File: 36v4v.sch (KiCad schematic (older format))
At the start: 47 parts, among them J1 Conn_01x03, J2 Conn_01x02, J3 Conn_01x02, J4 Conn_01x02, J5 Conn_01x02, J6 Conn_01x02, J7 Conn_01x02, U1 InnoSwitch3-CE, INN3162C, inS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

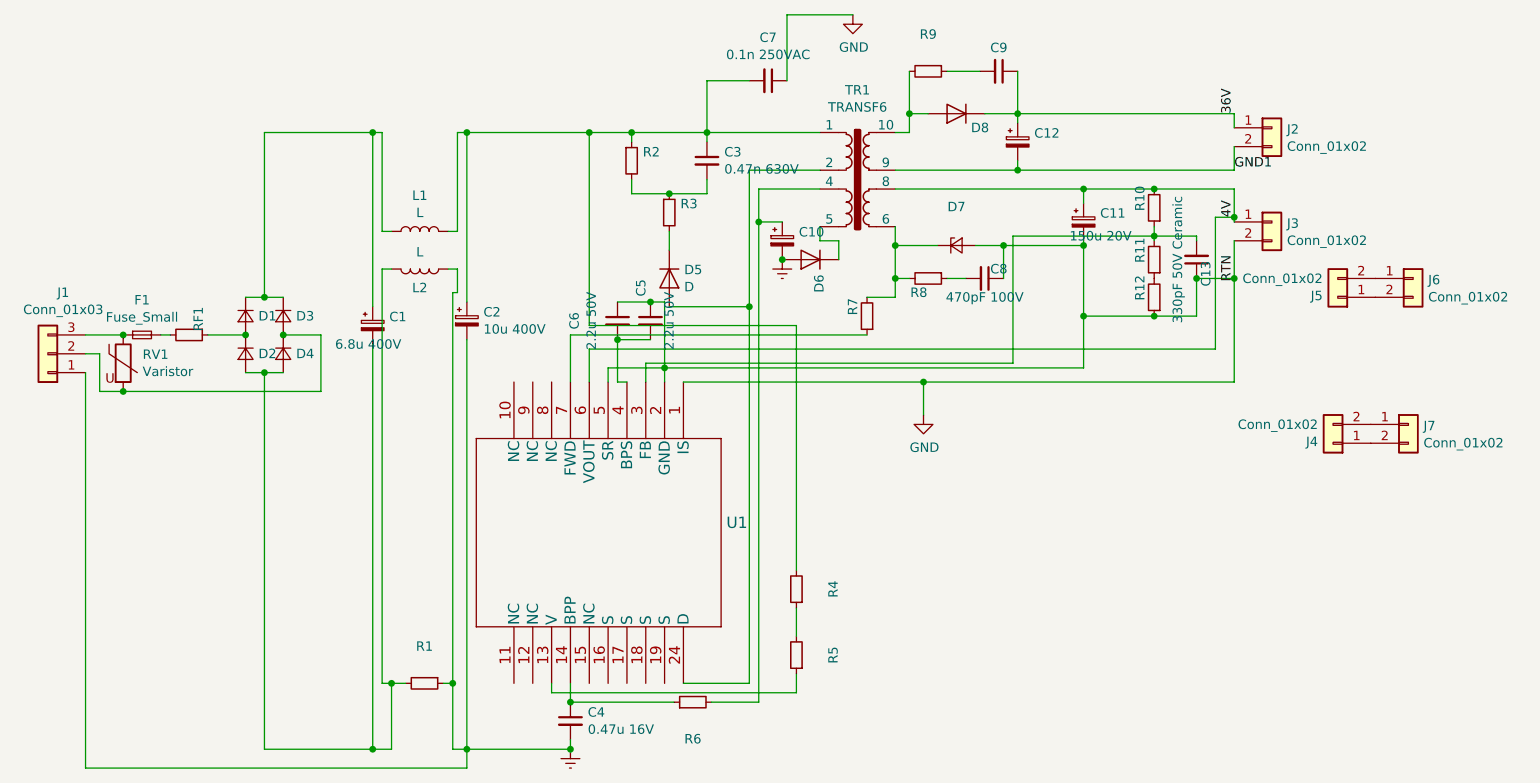
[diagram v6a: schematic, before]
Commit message: Rotated U1 in schematic to make primary/secondary clearer
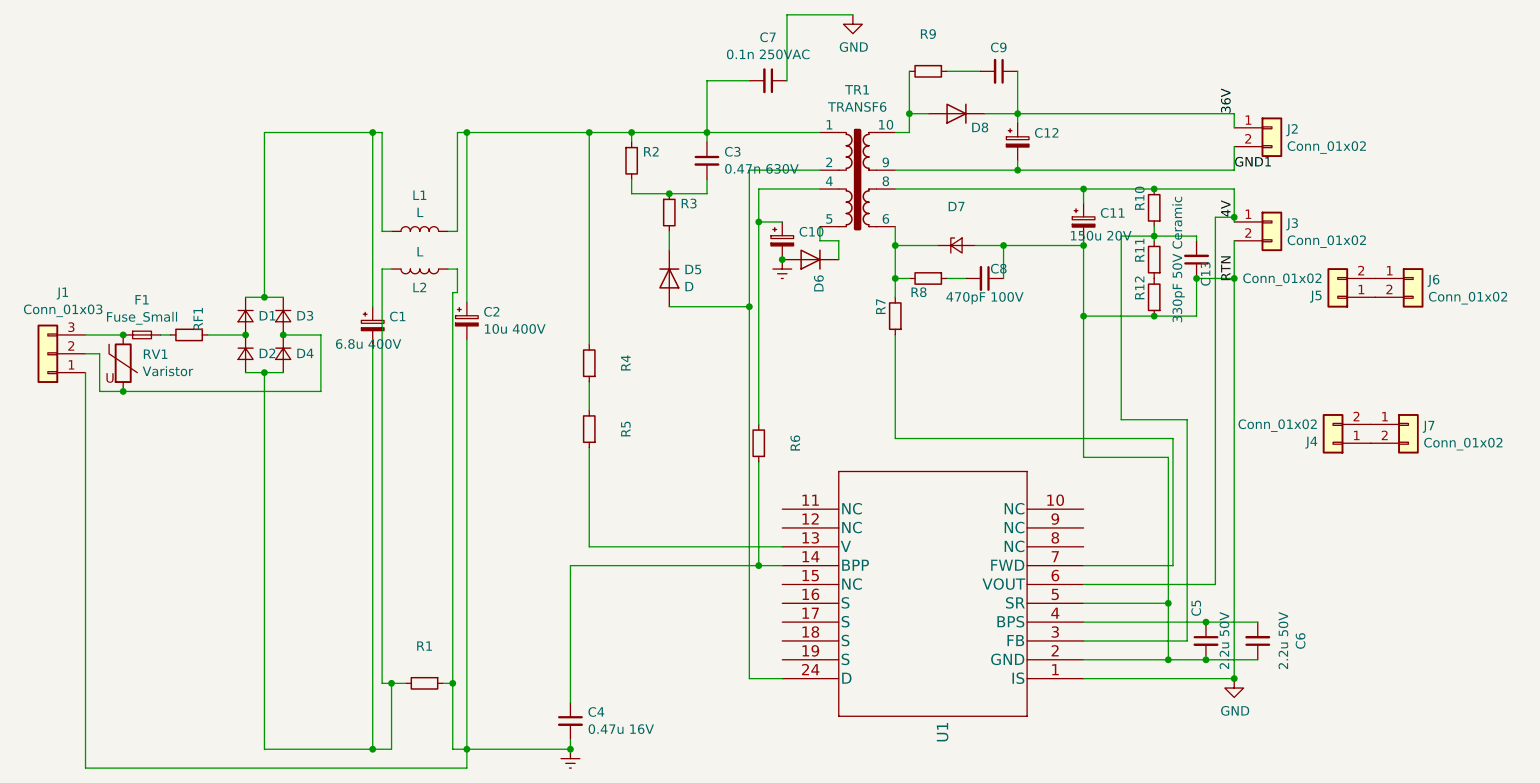
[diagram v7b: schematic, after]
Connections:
- net GND: now also C5.2; no longer C5.1
- net at C6.2, U1.4 (BPS): now also C5.1; no longer C5.2
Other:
- moved on the sheet: C5, C6, R4, R5, R6, R7
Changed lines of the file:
@@
 L Device:R_Small R7
 U 1 1 5E4F71AC
-P 6025 2425
-F 0 "R7" V 6100 2375 50  0000 C CNN
-F 1 "47 Ω, 5 %, 0.125 W, Carbon Film" V 5920 2425 50  0001 C CNN
-F 2 "Resistor_SMD:R_0603_1608Metric_Pad1.05x0.95mm_HandSolder" H 6025 2425 50  0001 C CNN
-F 3 "~" H 6025 2425 50  0001 C CNN
-	1    6025 2425
+P 6175 2425
+F 0 "R7" V 6250 2375 50  0000 C CNN
+F 1 "47 Ω, 5 %, 0.125 W, Carbon Film" V 6070 2425 50  0001 C CNN
+F 2 "Resistor_SMD:R_0603_1608Metric_Pad1.05x0.95mm_HandSolder" H 6175 2425 50  0001 C CNN
+F 3 "~" H 6175 2425 50  0001 C CNN
+	1    6175 2425
 	-1   0    0    1
 $EndComp
@@
 Text Label 7975 2100 3    50   ~ 0
 RTN
-$Comp
-L 2020-03-04_17-44-24:INN3162C-H1XX U1
-U 1 1 5E60AC5A
-P 5050 2775
-F 0 "U1" V 5797 3003 60  0000 L CNN
-F 1 "InnoSwitch3-CE, INN3162C, inSOP-24D" V 5903 3003 60  0001 L CNN
-F 2 "footprints:INN3162C-H1XX" H 5850 3015 60  0001 C CNN
-F 3 "" H 5050 2775 60  0000 C CNN
-F 4 "Power Integrations" H 5050 2775 50  0001 C CNN "MFG Name"
-F 5 "INN3162C-H101" H 5050 2775 50  0001 C CNN "MFG Part Num"
-	1    5050 2775
-	0    1    1    0
-$EndComp
 Wire Wire Line
 	3900 4725 4450 4725
@@
 Connection ~ 3900 4725
 Wire Wire Line
-	4450 4475 4450 4375
-Wire Wire Line
 	3900 2550 3900 4725
 Wire Wire Line
 	3400 2575 3400 4725
-Wire Wire Line
-	5050 4375 5400 4375
-Wire Wire Line
-	5400 4375 5400 2375
 $Comp
 L Device:R_Small R5
 U 1 1 5E66D184
-P 5650 4225
-F 0 "R5" V 5454 4225 50  0000 C CNN
-F 1 "1.78 MΩ, 1 %, 0.25 W, Metal Film" V 5545 4225 50  0001 C CNN
-F 2 "Resistor_SMD:R_0805_2012Metric_Pad1.15x1.40mm_HandSolder" H 5650 4225 50  0001 C CNN
-F 3 "~" H 5650 4225 50  0001 C CNN
-	1    5650 4225
+P 4550 3025
+F 0 "R5" V 4354 3025 50  0000 C CNN
+F 1 "1.78 MΩ, 1 %, 0.25 W, Metal Film" V 4445 3025 50  0001 C CNN
+F 2 "Resistor_SMD:R_0805_2012Metric_Pad1.15x1.40mm_HandSolder" H 4550 3025 50  0001 C CNN
+F 3 "~" H 4550 3025 50  0001 C CNN
+	1    4550 3025
 	-1   0    0    1
 $EndComp
@@
 L Device:R_Small R4
 U 1 1 5E66D7F4
-P 5650 3875
-F 0 "R4" V 5454 3875 50  0000 C CNN
-F 1 "1.78 MΩ, 1 %, 0.25 W, Metal Film" V 5545 3875 50  0001 C CNN
-F 2 "Resistor_SMD:R_0805_2012Metric_Pad1.15x1.40mm_HandSolder" H 5650 3875 50  0001 C CNN
-F 3 "~" H 5650 3875 50  0001 C CNN
-	1    5650 3875
-	-1   0    0    1
-$EndComp
-Wire Wire Line
-	5650 4125 5650 3975
-Wire Wire Line
-	5650 3775 5650 2475
-Wire Wire Line
-	5650 2475 4550 2475
-Wire Wire Line
-	4550 2475 4550 1450
+P 4550 2675
+F 0 "R4" V 4354 2675 50  0000 C CNN
+F 1 "1.78 MΩ, 1 %, 0.25 W, Metal Film" V 4445 2675 50  0001 C CNN
+F 2 "Resistor_SMD:R_0805_2012Metric_Pad1.15x1.40mm_HandSolder" H 4550 2675 50  0001 C CNN
+F 3 "~" H 4550 2675 50  0001 C CNN
+	1    4550 2675
+	-1   0    0    1
+$EndComp
+Wire Wire Line
+	4550 2925 4550 2775
 Connection ~ 4550 1450
 Wire Wire Line
 	4550 1450 4775 1450
-Wire Wire Line
-	4350 4375 4350 4425
-Wire Wire Line
-	4350 4425 5650 4425
-Wire Wire Line
-	5650 4425 5650 4325
 $Comp
 L Device:R_Small R6
 U 1 1 5E68331A
-P 5100 4475
-F 0 "R6" V 4904 4475 50  0000 C CNN
-F 1 "14 kΩ, 1 %, 0.125 W, Metal Film" V 4995 4475 50  0001 C CNN
-F 2 "Resistor_SMD:R_0805_2012Metric_Pad1.15x1.40mm_HandSolder" H 5100 4475 50  0001 C CNN
-F 3 "~" H 5100 4475 50  0001 C CNN
-	1    5100 4475
-	0    -1   -1   0
-$EndComp
-Wire Wire Line
-	4450 4475 5000 4475
-Connection ~ 4450 4475
-Wire Wire Line
-	5200 4475 5450 4475
-Wire Wire Line
-	5450 4475 5450 1925
+P 5450 3100
+F 0 "R6" V 5254 3100 50  0000 C CNN
+F 1 "14 kΩ, 1 %, 0.125 W, Metal Film" V 5345 3100 50  0001 C CNN
+F 2 "Resistor_SMD:R_0805_2012Metric_Pad1.15x1.40mm_HandSolder" H 5450 3100 50  0001 C CNN
+F 3 "~" H 5450 3100 50  0001 C CNN
+	1    5450 3100
+	-1   0    0    1
+$EndComp
+Wire Wire Line
+	5450 3750 5450 3200
 $Comp
 L Device:CP_Small C10
@@
 	6825 1350 7975 1350
 Wire Wire Line
-	4550 2775 4550 2600
-Wire Wire Line
-	4550 2600 7875 2600
-Wire Wire Line
-	7875 2600 7875 1900
-Wire Wire Line
 	7875 1900 7975 1900
 Wire Wire Line
@@
 	6600 2050 6750 2050
 Wire Wire Line
-	4450 2775 4450 2525
-Wire Wire Line
-	4450 2525 6025 2525
-Wire Wire Line
-	6025 2325 6175 2325
-Wire Wire Line
 	6175 2325 6175 2225
 Connection ~ 6175 2225
@@
 Connection ~ 6750 2050
 Connection ~ 7175 2050
-Wire Wire Line
-	4950 2700 7175 2700
-Wire Wire Line
-	4950 2775 4950 2700
-Wire Wire Line
-	4650 2775 4650 2700
-Wire Wire Line
-	4650 2700 4950 2700
-Connection ~ 4950 2700
 $Comp
 L Device:C_Small C5
 U 1 1 5E6F48CD
-P 4875 2450
-F 0 "C5" V 4825 2625 50  0000 C CNN
-F 1 "2.2u 50V" V 4975 2450 50  0000 C CNN
-F 2 "Capacitor_SMD:C_0603_1608Metric_Pad1.05x0.95mm_HandSolder" H 4875 2450 50  0001 C CNN
-F 3 "~" H 4875 2450 50  0001 C CNN
-F 4 "Murata/Kemet" H 4875 2450 50  0001 C CNN "MFG Name"
-F 5 "GRM188R61H225KE11D/C340C225K5R5TA" H 4875 2450 50  0001 C CNN "MFG Part Num"
-	1    4875 2450
+P 7825 4150
+F 0 "C5" V 7775 4325 50  0000 C CNN
+F 1 "2.2u 50V" V 7925 4150 50  0000 C CNN
+F 2 "Capacitor_SMD:C_0603_1608Metric_Pad1.05x0.95mm_HandSolder" H 7825 4150 50  0001 C CNN
+F 3 "~" H 7825 4150 50  0001 C CNN
+F 4 "Murata/Kemet" H 7825 4150 50  0001 C CNN "MFG Name"
+F 5 "GRM188R61H225KE11D/C340C225K5R5TA" H 7825 4150 50  0001 C CNN "MFG Part Num"
+	1    7825 4150
 	1    0    0    -1
 $EndComp
@@
 Wire Wire Line
 	7975 2025 7975 2225
-Wire Wire Line
-	7550 2000 6800 2000
-Wire Wire Line
-	6800 2000 6800 2675
-Wire Wire Line
-	6800 2675 4850 2675
-Wire Wire Line
-	4850 2675 4850 2775
 Connection ~ 7550 2000
 Wire Wire Line
@@
 L power:GND #PWR0104
 U 1 1 5E73A9AA
-P 6325 2950
-F 0 "#PWR0104" H 6325 2700 50  0001 C CNN
-F 1 "GND" H 6330 2777 50  0000 C CNN
-F 2 "" H 6325 2950 50  0001 C CNN
-F 3 "" H 6325 2950 50  0001 C CNN
-	1    6325 2950
-	1    0    0    -1
-$EndComp
-Wire Wire Line
-	5050 2775 6325 2775
-Wire Wire Line
-	6325 2775 6325 2950
-Wire Wire Line
-	6325 2775 7975 2775
-Wire Wire Line
-	7975 2775 7975 2225
-Connection ~ 6325 2775
+P 7975 4350
+F 0 "#PWR0104" H 7975 4100 50  0001 C CNN
+F 1 "GND" H 7980 4177 50  0000 C CNN
+F 2 "" H 7975 4350 50  0001 C CNN
+F 3 "" H 7975 4350 50  0001 C CNN
+	1    7975 4350
+	1    0    0    -1
+$EndComp
 Connection ~ 7975 2225
 Wire Wire Line
@@
 Wire Wire Line
 	5450 1750 5775 1750
-Connection ~ 5450 1925
 Wire Wire Line
 	5775 1950 5775 2025
@@
 Wire Wire Line
 	5400 1650 5775 1650
-Connection ~ 5400 2375
 $Comp
 L xformers:TRANSF6 TR1
@@
 Connection ~ 7175 2425
 Wire Wire Line
-	7175 2425 7175 2700
-Wire Wire Line
 	7775 2225 7775 2425
 Wire Wire Line
@@
 L Device:C_Small C6
 U 1 1 5E9E2EF2
-P 4700 2450
-F 0 "C6" V 4471 2450 50  0000 C CNN
-F 1 "2.2u 50V" V 4562 2450 50  0000 C CNN
-F 2 "Capacitor_SMD:C_0603_1608Metric_Pad1.05x0.95mm_HandSolder" H 4700 2450 50  0001 C CNN
-F 3 "~" H 4700 2450 50  0001 C CNN
-F 4 "Murata/Kemet" H 4700 2450 50  0001 C CNN "MFG Name"
-F 5 "GRM188R61H225KE11D/C340C225K5R5TA" H 4700 2450 50  0001 C CNN "MFG Part Num"
-	1    4700 2450
-	1    0    0    -1
-$EndComp
-Wire Wire Line
-	4700 2550 4875 2550
-Wire Wire Line
-	4700 2550 4700 2775
-Wire Wire Line
-	4700 2775 4750 2775
-Connection ~ 4700 2550
-Wire Wire Line
-	4700 2350 4875 2350
-Wire Wire Line
-	4875 2350 4950 2350
-Wire Wire Line
-	4950 2350 4950 2700
-Connection ~ 4875 2350
+P 8100 4150
+F 0 "C6" V 7871 4150 50  0000 C CNN
+F 1 "2.2u 50V" V 7962 4150 50  0000 C CNN
+F 2 "Capacitor_SMD:C_0603_1608Metric_Pad1.05x0.95mm_HandSolder" H 8100 4150 50  0001 C CNN
+F 3 "~" H 8100 4150 50  0001 C CNN
+F 4 "Murata/Kemet" H 8100 4150 50  0001 C CNN "MFG Name"
+F 5 "GRM188R61H225KE11D/C340C225K5R5TA" H 8100 4150 50  0001 C CNN "MFG Part Num"
+	1    8100 4150
+	-1   0    0    1
+$EndComp
 $Comp
 L Device:D_Small D1
@@
 	1    0    0    -1
 $EndComp
+$Comp
+L 2020-03-04_17-44-24:INN3162C-H1XX U1
+U 1 1 5E9BC18A
+P 7175 4350
+F 0 "U1" V 7922 4578 60  0000 L CNN
+F 1 "InnoSwitch3-CE, INN3162C, inSOP-24D" V 8028 4578 60  0001 L CNN
+F 2 "footprints:INN3162C-H1XX" H 7975 4590 60  0001 C CNN
+F 3 "" H 7175 4350 60  0000 C CNN
+F 4 "Power Integrations" H 7175 4350 50  0001 C CNN "MFG Name"
+F 5 "INN3162C-H101" H 7175 4350 50  0001 C CNN "MFG Part Num"
+	1    7175 4350
+	-1   0    0    1
+$EndComp
+Connection ~ 7975 4350
+Wire Wire Line
+	7975 2225 7975 4350
+Wire Wire Line
+	7625 3950 7625 4250
+Wire Wire Line
+	6175 2525 6175 3075
+Wire Wire Line
+	6175 3075 7650 3075
+Wire Wire Line
+	7650 3075 7650 3750
+Wire Wire Line
+	7875 1900 7875 3850
+Wire Wire Line
+	7550 2000 7375 2000
+Wire Wire Line
+	7375 2000 7375 2975
+Wire Wire Line
+	7375 2975 7725 2975
+Wire Wire Line
+	7725 2975 7725 4150
+Wire Wire Line
+	7825 4050 8100 4050
+Connection ~ 7825 4050
+Wire Wire Line
+	8100 4250 7825 4250
+Wire Wire Line
+	7825 4250 7625 4250
+Connection ~ 7825 4250
+Connection ~ 7625 4250
+Wire Wire Line
+	7175 3175 7625 3175
+Wire Wire Line
+	7625 3175 7625 3950
+Wire Wire Line
+	7175 2425 7175 3175
+Connection ~ 7625 3950
+Wire Wire Line
+	4550 3125 4550 3650
+Wire Wire Line
+	5400 2375 5400 4350
+Connection ~ 5400 2375
+Connection ~ 5450 1925
+Wire Wire Line
+	5450 1925 5450 3000
+Wire Wire Line
+	4450 4475 4450 3750
+Wire Wire Line
+	4450 3750 5450 3750
+Wire Wire Line
+	4550 1450 4550 2575
+Wire Wire Line
+	5400 4350 5575 4350
+Wire Wire Line
+	4550 3650 5575 3650
+Wire Wire Line
+	5450 3750 5575 3750
+Connection ~ 5450 3750
+Wire Wire Line
+	7175 3750 7650 3750
+Wire Wire Line
+	7175 3850 7875 3850
+Wire Wire Line
+	7175 3950 7625 3950
+Wire Wire Line
+	7175 4050 7825 4050
+Wire Wire Line
+	7175 4150 7725 4150
+Wire Wire Line
+	7175 4250 7625 4250
+Wire Wire Line
+	7175 4350 7975 4350
 $EndSCHEMATC

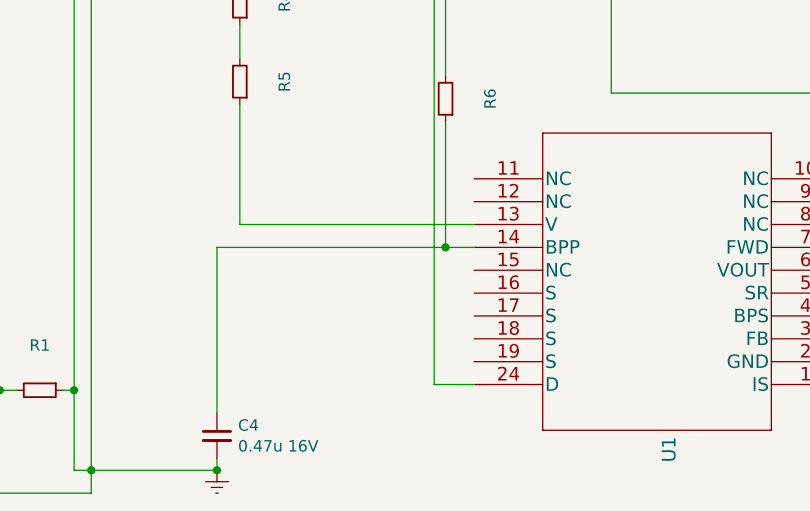
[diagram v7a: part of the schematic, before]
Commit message: Maximize hatched area for heat sinking
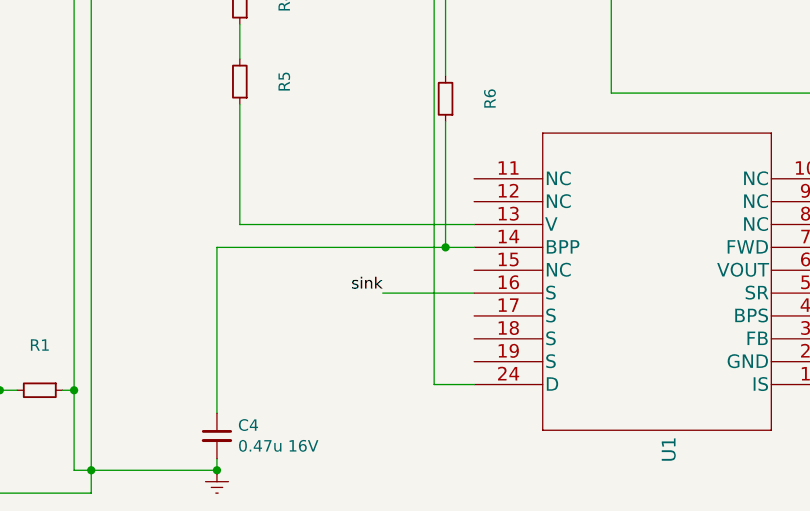
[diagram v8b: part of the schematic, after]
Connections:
- net sink: now reaches U1.16 (S)
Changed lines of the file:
@@
 Wire Wire Line
 	7175 4350 7975 4350
+Text Label 5175 3950 2    50   ~ 0
+sink
+Wire Wire Line
+	5175 3950 5575 3950
 $EndSCHEMATC
